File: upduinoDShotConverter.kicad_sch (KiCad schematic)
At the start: 17 parts, among them J1 ESC_OUT, J10 Conn_02x05_Odd_Even, J2 5V and Buzzer In, J3 VBAT_and_motors_1-4_in, J4 Conn_01x24_Pin, J5 Motors_5-8_in, J6 Conn_01x24_Pin, J7 Conn_01x12_Socket, J8 Conn_01x03_Pin, J9 Conn_01x02_Pin

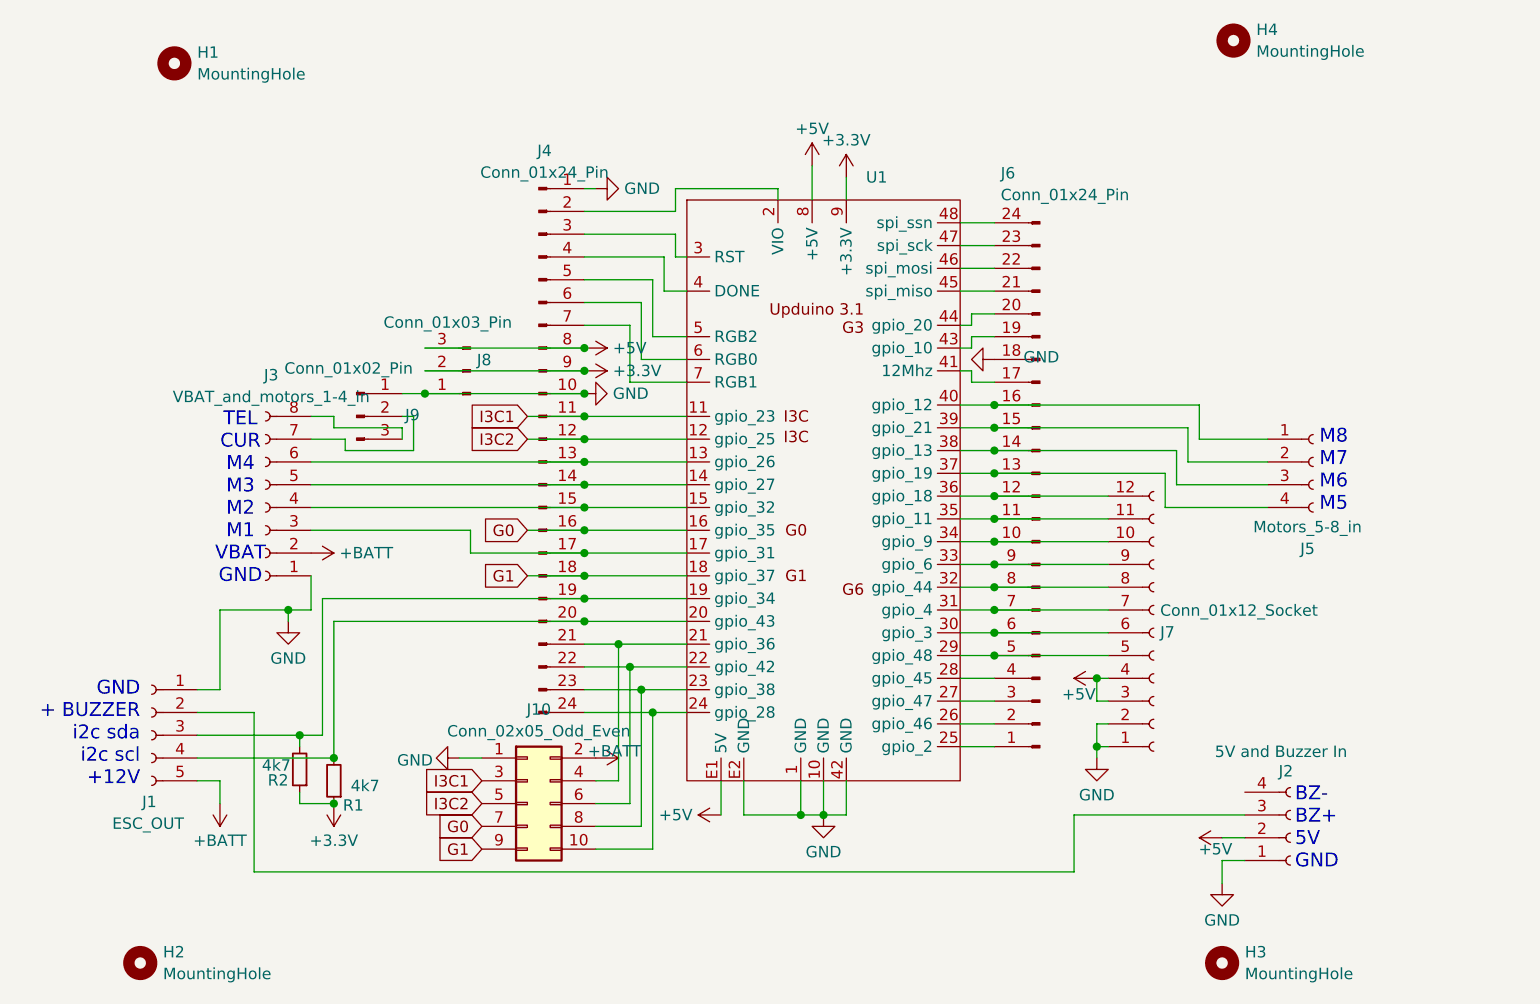
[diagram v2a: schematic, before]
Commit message: finalize design for v1.0 release, and assign parts from LCSC/JLCPCB
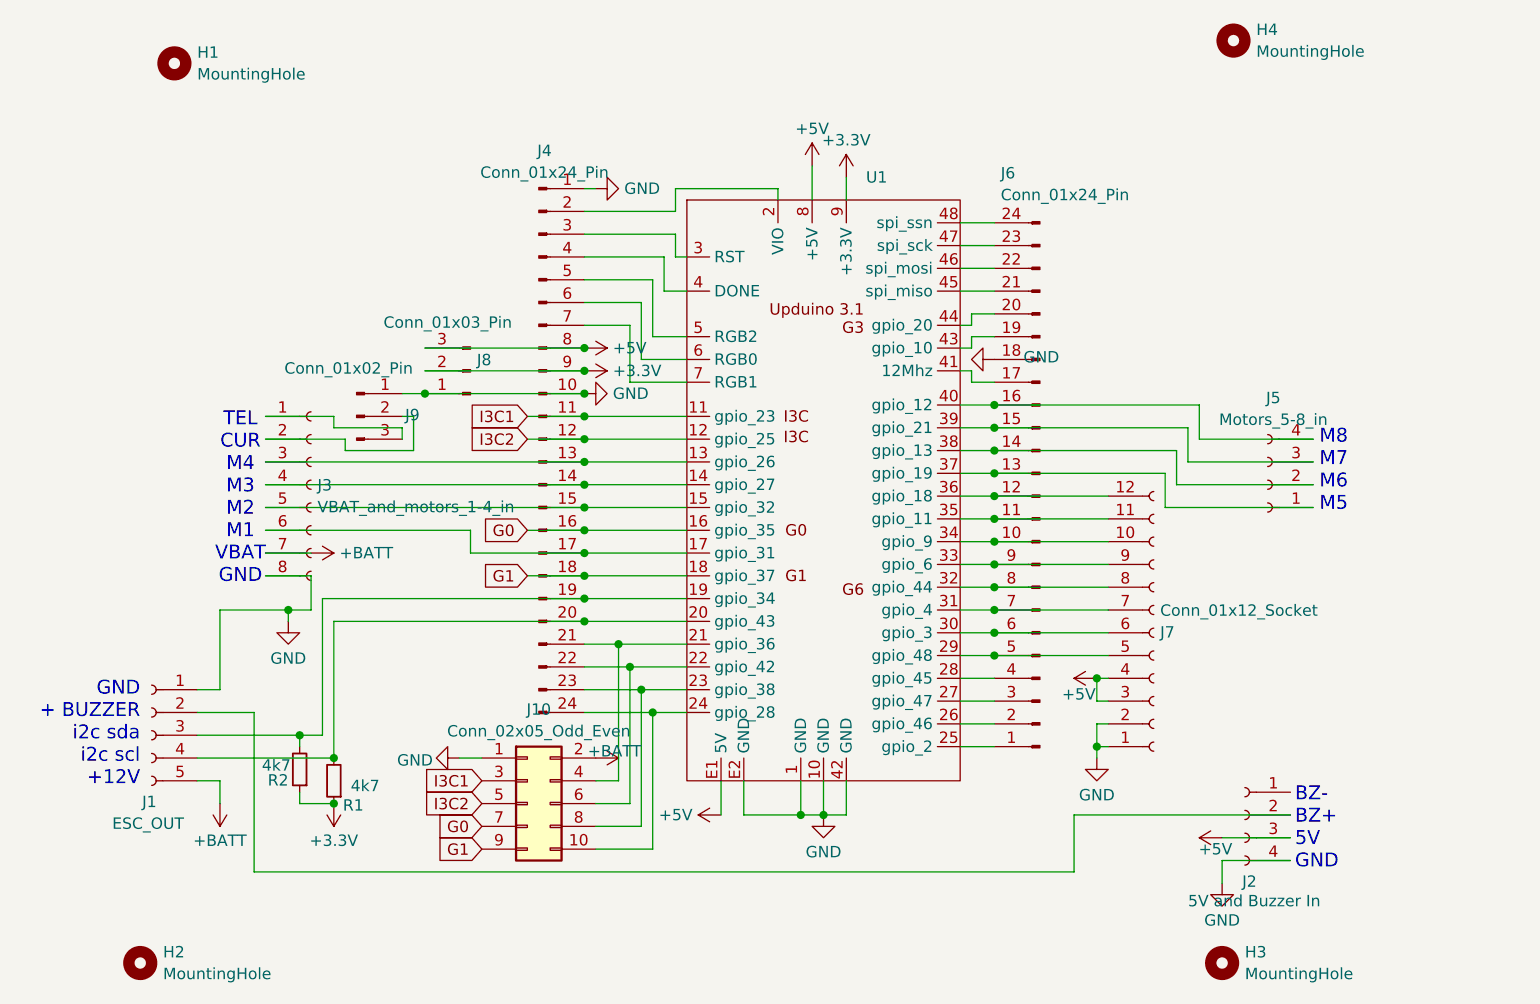
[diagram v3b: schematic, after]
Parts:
- J1: LCSC (none) -> C392176
- J2, J5: footprint Connector_JST:JST_SH_BM04B-SRSS-TB_1x04-1MP_P1.00mm_Vertical -> Connector_JST:JST_SH_SM04B-SRSS-TB_1x04-1MP_P1.00mm_Horizontal; LCSC (none) -> C160404
- J3: footprint Connector_JST:JST_SH_BM08B-SRSS-TB_1x08-1MP_P1.00mm_Vertical -> Connector_JST:JST_SH_SM08B-SRSS-TB_1x08-1MP_P1.00mm_Horizontal; LCSC (none) -> C160407
- J7: LCSC (none) -> C160411
- R1, R2: LCSC (none) -> C23162
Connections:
- net +5V: now also J2.3 (Pin_3); no longer J2.2 (Pin_2)
- net +BATT: now also J3.7 (Pin_7); no longer J3.2 (Pin_2)
- net GND: now also J2.4 (Pin_4), J3.8 (Pin_8); no longer J2.1 (Pin_1), J3.1 (Pin_1)
- net at J4.13 (Pin_13), U1.13 (gpio_26): now also J3.3 (Pin_3); no longer J3.6 (Pin_6)
- net at J4.14 (Pin_14), U1.14 (gpio_27): now also J3.4 (Pin_4); no longer J3.5 (Pin_5)
- net at J4.15 (Pin_15), U1.15 (gpio_32): now also J3.5 (Pin_5); no longer J3.4 (Pin_4)
- net at J4.17 (Pin_17), U1.17 (gpio_31): now also J3.6 (Pin_6); no longer J3.3 (Pin_3)
- net at J6.13 (Pin_13), U1.37 (gpio_19): now also J5.1 (Pin_1); no longer J5.4 (Pin_4)
- net at J6.14 (Pin_14), U1.38 (gpio_13): now also J5.2 (Pin_2); no longer J5.3 (Pin_3)
- net at J6.15 (Pin_15), U1.39 (gpio_21): now also J5.3 (Pin_3); no longer J5.2 (Pin_2)
- net at J6.16 (Pin_16), U1.40 (gpio_12): now also J5.4 (Pin_4); no longer J5.1 (Pin_1)
- net at J9.2 (Pin_2): now also J3.2 (Pin_2); no longer J3.7 (Pin_7)
- net at J9.3 (Pin_3): now also J3.1 (Pin_1); no longer J3.8 (Pin_8)
- net at J1.2 (Pin_2): now also J2.2 (Pin_2); no longer J2.3 (Pin_3)
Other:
- moved on the sheet: J3, J5
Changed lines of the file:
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@@
 	(wire
 		(pts
+			(xy 81.28 87.63) (xy 90.17 87.63)
+		)
+		(stroke
+			(width 0)
+			(type default)
+		)
+	)
+	(wire
+		(pts
 			(xy 110.49 97.79) (xy 116.84 97.79)
 		)
@@
 	(wire
 		(pts
-			(xy 193.04 90.17) (xy 184.15 90.17)
+			(xy 184.15 90.17) (xy 198.12 90.17)
 		)
 		(stroke
@@
 	(wire
 		(pts
-			(xy 193.04 87.63) (xy 185.42 87.63)
+			(xy 185.42 87.63) (xy 198.12 87.63)
 		)
 		(stroke
@@
 	(wire
 		(pts
+			(xy 81.28 102.87) (xy 86.36 102.87)
+		)
+		(stroke
+			(width 0)
+			(type default)
+		)
+	)
+	(wire
+		(pts
 			(xy 173.99 116.84) (xy 173.99 114.3)
 		)
@@
 	(wire
 		(pts
-			(xy 193.04 95.25) (xy 181.61 95.25)
+			(xy 181.61 95.25) (xy 198.12 95.25)
 		)
 		(stroke
@@
 	(wire
 		(pts
-			(xy 118.11 125.73) (xy 120.65 125.73)
+			(xy 81.28 85.09) (xy 88.9 85.09)
 		)
 		(stroke
@@
 	(wire
 		(pts
-			(xy 76.2 125.73) (xy 73.66 125.73)
+			(xy 118.11 125.73) (xy 120.65 125.73)
 		)
 		(stroke
@@
 	(wire
 		(pts
-			(xy 173.99 121.92) (xy 173.99 123.19)
+			(xy 76.2 125.73) (xy 73.66 125.73)
 		)
 		(stroke
@@
 	(wire
 		(pts
-			(xy 184.15 90.17) (xy 184.15 86.36)
+			(xy 173.99 121.92) (xy 173.99 123.19)
 		)
 		(stroke
@@
 	(wire
 		(pts
-			(xy 86.36 85.09) (xy 88.9 85.09)
+			(xy 184.15 90.17) (xy 184.15 86.36)
 		)
 		(stroke
@@
 	(wire
 		(pts
-			(xy 193.04 92.71) (xy 182.88 92.71)
+			(xy 182.88 92.71) (xy 198.12 92.71)
 		)
 		(stroke
@@
 	(wire
 		(pts
+			(xy 81.28 92.71) (xy 116.84 92.71)
+		)
+		(stroke
+			(width 0)
+			(type default)
+		)
+	)
+	(wire
+		(pts
 			(xy 146.05 58.42) (xy 146.05 60.96)
 		)
@@
 	(wire
 		(pts
-			(xy 190.5 129.54) (xy 171.45 129.54)
+			(xy 171.45 129.54) (xy 195.58 129.54)
 		)
 		(stroke
@@
 	(wire
 		(pts
-			(xy 190.5 134.62) (xy 187.96 134.62)
+			(xy 187.96 134.62) (xy 195.58 134.62)
 		)
 		(stroke
@@
 	(wire
 		(pts
-			(xy 86.36 90.17) (xy 116.84 90.17)
+			(xy 86.36 102.87) (xy 86.36 106.68)
 		)
 		(stroke
@@
 	(wire
 		(pts
-			(xy 86.36 102.87) (xy 86.36 106.68)
+			(xy 127 64.77) (xy 127 67.31)
 		)
 		(stroke
@@
 	(wire
 		(pts
-			(xy 127 64.77) (xy 127 67.31)
+			(xy 158.75 93.98) (xy 162.56 93.98)
 		)
 		(stroke
@@
 	(wire
 		(pts
-			(xy 158.75 93.98) (xy 162.56 93.98)
+			(xy 81.28 95.25) (xy 116.84 95.25)
 		)
 		(stroke
@@
 	(wire
 		(pts
-			(xy 120.65 125.73) (xy 120.65 110.49)
+			(xy 81.28 100.33) (xy 86.36 100.33)
 		)
 		(stroke
@@
 	(wire
 		(pts
-			(xy 88.9 107.95) (xy 116.84 107.95)
+			(xy 120.65 125.73) (xy 120.65 110.49)
 		)
 		(stroke
@@
 	(wire
 		(pts
-			(xy 86.36 97.79) (xy 104.14 97.79)
+			(xy 88.9 107.95) (xy 116.84 107.95)
 		)
 		(stroke
@@
 	(wire
 		(pts
+			(xy 81.28 97.79) (xy 104.14 97.79)
+		)
+		(stroke
+			(width 0)
+			(type default)
+		)
+	)
+	(wire
+		(pts
 			(xy 142.24 57.15) (xy 142.24 60.96)
 		)
@@
 	(wire
 		(pts
-			(xy 86.36 95.25) (xy 116.84 95.25)
-		)
-		(stroke
-			(width 0)
-			(type default)
-		)
-	)
-	(wire
-		(pts
 			(xy 85.09 128.27) (xy 88.9 128.27)
 		)
@@
 	(wire
 		(pts
-			(xy 86.36 87.63) (xy 90.17 87.63)
+			(xy 81.28 90.17) (xy 116.84 90.17)
 		)
 		(stroke
@@
 	(wire
 		(pts
-			(xy 187.96 132.08) (xy 190.5 132.08)
-		)
-		(stroke
-			(width 0)
-			(type default)
-		)
-	)
-	(wire
-		(pts
-			(xy 86.36 92.71) (xy 116.84 92.71)
+			(xy 187.96 132.08) (xy 195.58 132.08)
 		)
 		(stroke
@@
 			)
 		)
+		(property "LCSC" "C23162"
+			(at 92.2274 128.4662 0)
+			(effects
+				(font
+					(size 1.27 1.27)
+				)
+				(hide yes)
+			)
+		)
 		(pin "2"
 		)
@@
 	(symbol
 		(lib_id "Connector:Conn_01x08_Socket")
-		(at 81.28 95.25 180)
+		(at 86.36 92.71 0)
 		(unit 1)
 		(exclude_from_sim no)
@@
 		(fields_autoplaced yes)
 		(property "Reference" "J3"
-			(at 81.915 80.4883 0)
+			(at 87.0712 92.7678 0)
 			(effects
 				(font
 					(size 1.27 1.27)
 				)
+				(justify left)
 			)
 		)
 		(property "Value" "VBAT_and_motors_1-4_in"
-			(at 81.915 82.9126 0)
+			(at 87.0712 95.1921 0)
 			(effects
 				(font
 					(size 1.27 1.27)
 				)
+				(justify left)
 			)
 		)
-		(property "Footprint" "Connector_JST:JST_SH_BM08B-SRSS-TB_1x08-1MP_P1.00mm_Vertical"
-			(at 81.28 95.25 0)
+		(property "Footprint" "Connector_JST:JST_SH_SM08B-SRSS-TB_1x08-1MP_P1.00mm_Horizontal"
+			(at 86.36 92.71 0)
 			(effects
 				(font
@@
 		)
 		(property "Datasheet" "~"
-			(at 81.28 95.25 0)
+			(at 86.36 92.71 0)
 			(effects
 				(font
@@
 		)
 		(property "Description" "Generic connector, single row, 01x08, script generated"
-			(at 81.28 95.25 0)
+			(at 86.36 92.71 0)
+			(effects
+				(font
+					(size 1.27 1.27)
+				)
+				(hide yes)
+			)
+		)
+		(property "LCSC" "C160407"
+			(at 87.0712 92.7678 0)
 			(effects
 				(font
@@
 			)
 		)
+		(property "LCSC" "C23162"
+			(at 83.8454 125.6722 0)
+			(effects
+				(font
+					(size 1.27 1.27)
+				)
+				(hide yes)
+			)
+		)
 		(pin "2"
 		)
@@
 	(symbol
 		(lib_id "Connector:Conn_01x04_Socket")
-		(at 198.12 90.17 0)
+		(at 193.04 92.71 180)
 		(unit 1)
 		(exclude_from_sim no)
@@
 		(fields_autoplaced yes)
 		(property "Reference" "J5"
-			(at 197.485 99.8517 0)
+			(at 193.675 83.0283 0)
 			(effects
 				(font
@@
 		)
 		(property "Value" "Motors_5-8_in"
-			(at 197.485 97.4274 0)
+			(at 193.675 85.4526 0)
 			(effects
 				(font
@@
 			)
 		)
-		(property "Footprint" "Connector_JST:JST_SH_BM04B-SRSS-TB_1x04-1MP_P1.00mm_Vertical"
-			(at 198.12 90.17 0)
+		(property "Footprint" "Connector_JST:JST_SH_SM04B-SRSS-TB_1x04-1MP_P1.00mm_Horizontal"
+			(at 193.04 92.71 0)
 			(effects
 				(font
@@
 		)
 		(property "Datasheet" "~"
-			(at 198.12 90.17 0)
+			(at 193.04 92.71 0)
 			(effects
 				(font
@@
 		)
 		(property "Description" "Generic connector, single row, 01x04, script generated"
-			(at 198.12 90.17 0)
+			(at 193.04 92.71 0)
+			(effects
+				(font
+					(size 1.27 1.27)
+				)
+				(hide yes)
+			)
+		)
+		(property "LCSC" "C160404"
+			(at 193.675 83.0283 0)
 			(effects
 				(font
@@
 			)
 		)
+		(property "LCSC" "C160411"
+			(at 181.0512 109.1622 0)
+			(effects
+				(font
+					(size 1.27 1.27)
+				)
+				(hide yes)
+			)
+		)
 		(pin "2"
 		)
@@
 	(symbol
 		(lib_id "Connector:Conn_01x04_Socket")
-		(at 195.58 132.08 0)
-		(mirror x)
+		(at 190.5 129.54 0)
+		(mirror y)
 		(unit 1)
 		(exclude_from_sim no)
@@
 		(dnp no)
 		(property "Reference" "J2"
-			(at 194.2592 124.6562 0)
+			(at 191.8208 136.9638 0)
 			(effects
 				(font
@@
 		)
 		(property "Value" "5V and Buzzer In"
-			(at 187.1472 122.4859 0)
+			(at 198.9328 139.1341 0)
 			(effects
 				(font
@@
 			)
 		)
-		(property "Footprint" "Connector_JST:JST_SH_BM04B-SRSS-TB_1x04-1MP_P1.00mm_Vertical"
-			(at 195.58 132.08 0)
+		(property "Footprint" "Connector_JST:JST_SH_SM04B-SRSS-TB_1x04-1MP_P1.00mm_Horizontal"
+			(at 190.5 129.54 0)
 			(effects
 				(font
@@
 		)
 		(property "Datasheet" "~"
-			(at 195.58 132.08 0)
+			(at 190.5 129.54 0)
 			(effects
 				(font
@@
 		)
 		(property "Description" "Generic connector, single row, 01x04, script generated"
-			(at 195.58 132.08 0)
+			(at 190.5 129.54 0)
+			(effects
+				(font
+					(size 1.27 1.27)
+				)
+				(hide yes)
+			)
+		)
+		(property "LCSC" "C160404"
+			(at 191.8208 136.9638 0)
 			(effects
 				(font
@@
 			(effects
 				(font
+					(size 1.27 1.27)
+				)
+				(hide yes)
+			)
+		)
+		(property "LCSC" "C392176"
+			(at 69.1388 128.0738 0)
+			(effects
+				(font
